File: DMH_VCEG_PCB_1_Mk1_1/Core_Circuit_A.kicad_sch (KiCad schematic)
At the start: 110 parts, among them J21 Conn_01x10_PinHeader, J22 Conn_01x10_PinHeader, J23 Conn_01x10_PinHeader, J24 Conn_01x06_PinHeader, Q1 BC558, Q10 BC548, Q2 BC558, Q3 BC548, Q4 BC548, Q5 BC548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

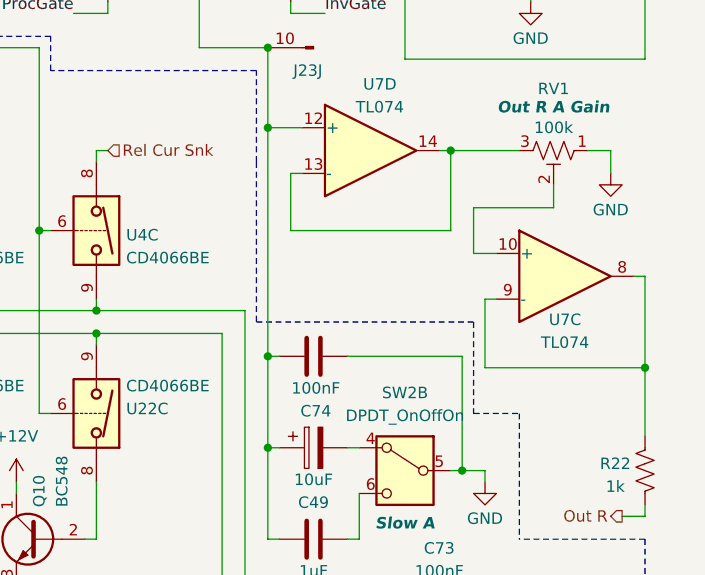
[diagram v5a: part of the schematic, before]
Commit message: Copied Out R redesign to Circuit B
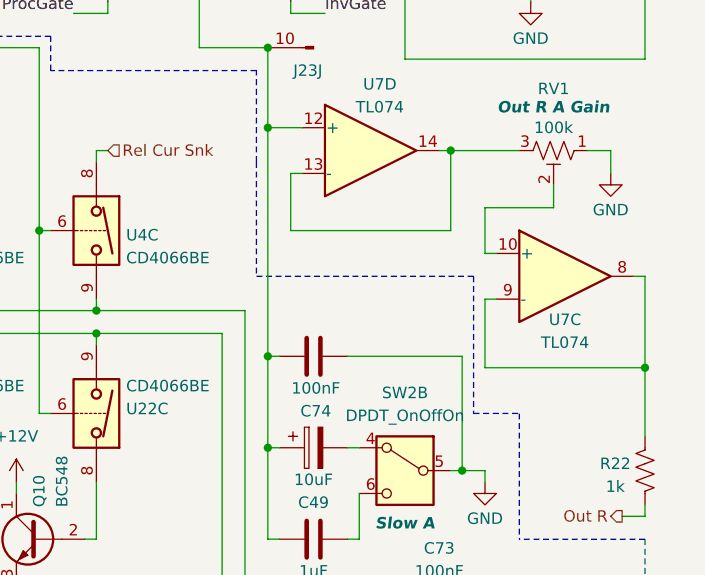
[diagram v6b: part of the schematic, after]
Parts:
- U26: footprint Package_DIP:DIP-14_W7.62mm -> Package_DIP:DIP-14_W7.62mm_Socket
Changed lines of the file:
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@@
 	(polyline
 		(pts
-			(xy 264.16 73.66) (xy 264.16 83.82)
+			(xy 264.16 68.58) (xy 264.16 83.82)
 		)
 		(stroke
@@
 	(polyline
 		(pts
-			(xy 264.16 73.66) (xy 240.03 73.66)
+			(xy 264.16 68.58) (xy 240.03 68.58)
 		)
 		(stroke
@@
 	(wire
 		(pts
-			(xy 264.16 66.04) (xy 266.7 66.04)
+			(xy 265.43 66.04) (xy 266.7 66.04)
 		)
 		(stroke
@@
 	(polyline
 		(pts
-			(xy 240.03 55.88) (xy 240.03 73.66)
+			(xy 240.03 55.88) (xy 240.03 68.58)
 		)
 		(stroke
@@
 	(wire
 		(pts
-			(xy 264.16 60.96) (xy 264.16 66.04)
+			(xy 265.43 60.96) (xy 265.43 66.04)
 		)
 		(stroke
@@
 	(wire
 		(pts
-			(xy 273.05 60.96) (xy 264.16 60.96)
+			(xy 273.05 60.96) (xy 265.43 60.96)
 		)
 		(stroke
@@
 		(exclude_from_sim no)
 		(in_bom yes)
-		(on_board no)
+		(on_board yes)
 		(dnp no)
 		(property "Reference" "U26"
@@
 			)
 		)
-		(property "Footprint" "Package_DIP:DIP-14_W7.62mm"
+		(property "Footprint" "Package_DIP:DIP-14_W7.62mm_Socket"
 			(at 243.84 35.56 0)
 			(effects
@@
 		(exclude_from_sim no)
 		(in_bom yes)
-		(on_board no)
+		(on_board yes)
 		(dnp no)
 		(property "Reference" "U26"
@@
 			)
 		)
-		(property "Footprint" "Package_DIP:DIP-14_W7.62mm"
+		(property "Footprint" "Package_DIP:DIP-14_W7.62mm_Socket"
 			(at 223.52 35.56 0)
 			(effects
